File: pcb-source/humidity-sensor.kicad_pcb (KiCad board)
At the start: 2 copper layers, 34.3 x 22.6 mm, 78 parts, among them J1 Conn_ARM_JTAG_SWD_10, J2 Conn_02x03_Odd_Even, Q1 Q_NMOS_GSD, Q2 Q_NMOS_GSD, U1 STM32L051C8Tx, U2 SHTC3, U3 SYN115, Y1 13.56MHz, Y2 DNU

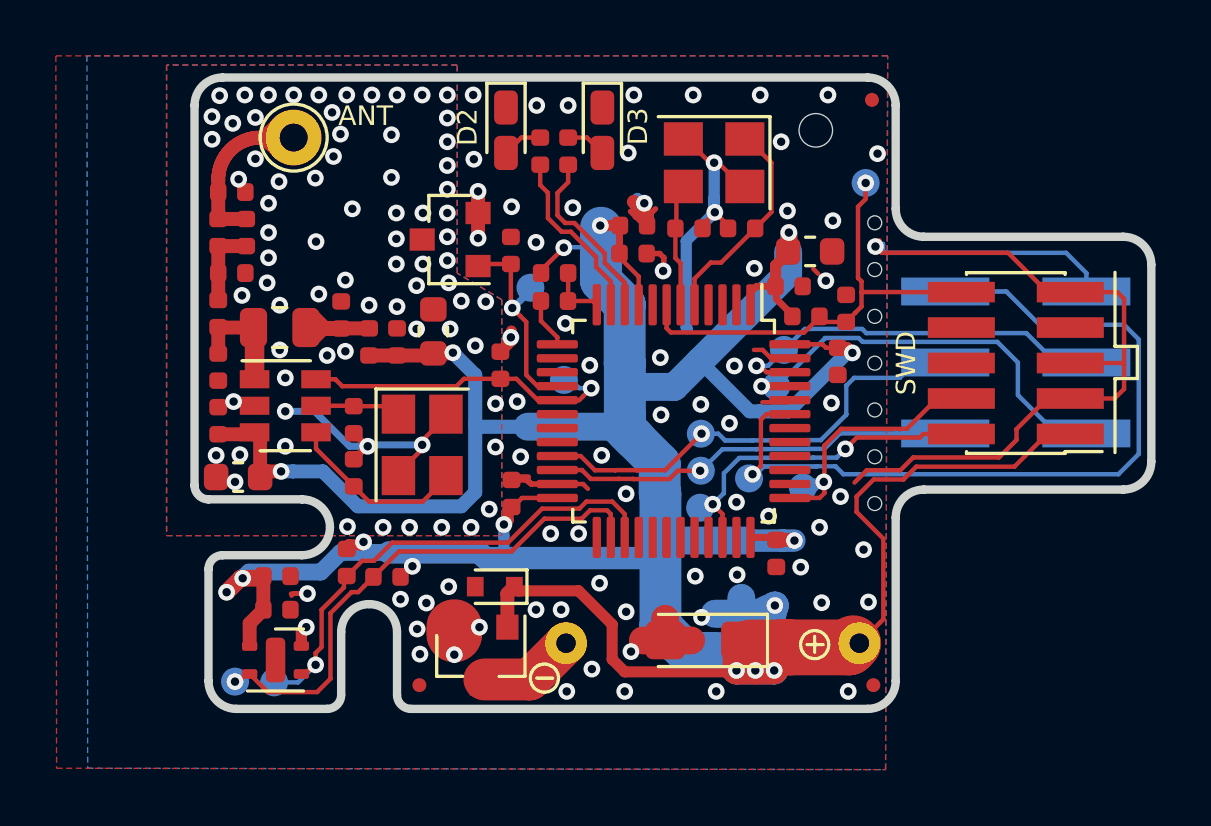
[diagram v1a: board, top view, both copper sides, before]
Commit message: Modify fiducials
Library footprint doesn't create copper pull-back from
soldermask opening.
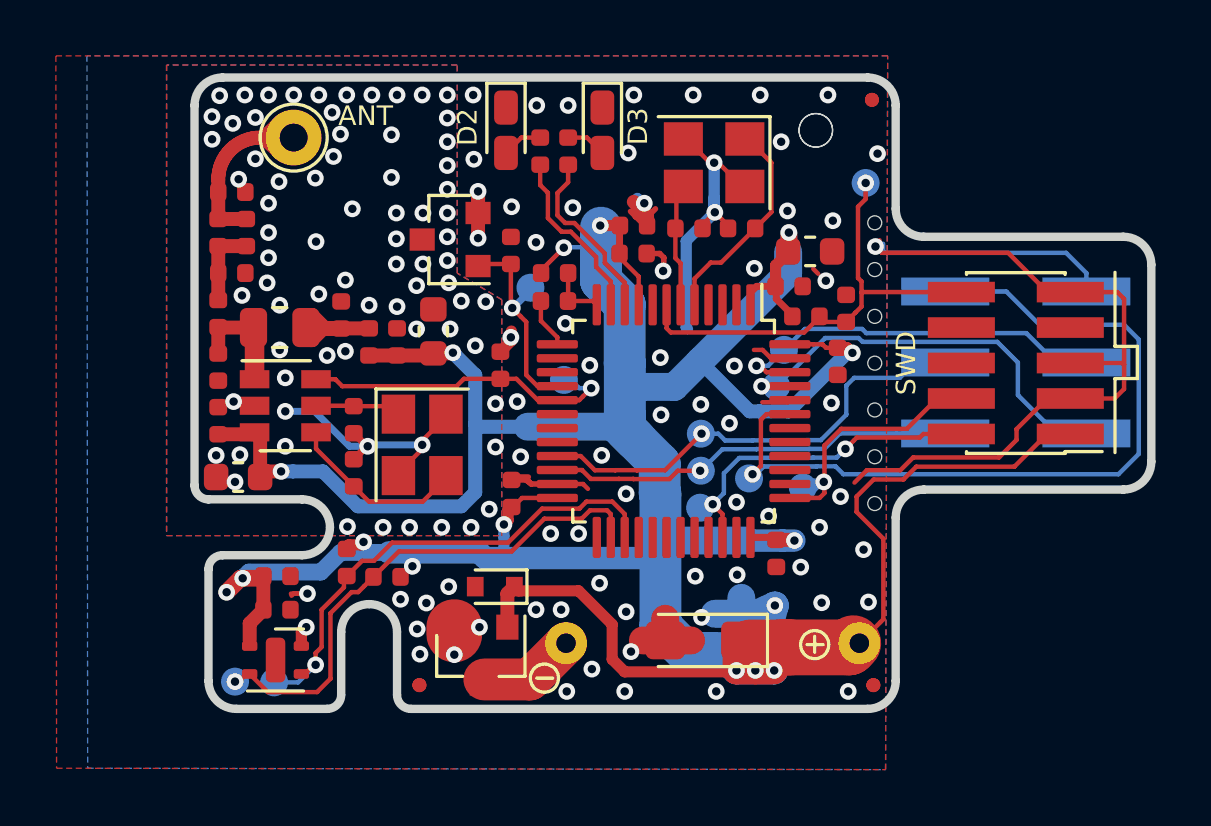
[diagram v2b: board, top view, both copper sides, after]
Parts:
- removed the FID1 at (62.7, 49.0)
- removed the FID2 at (79.0, 49.0)
- removed the FID3 at (78.9, 28.1)
- removed the REF** at (76.9, 29.2)
- added FID1 (x2): Fiducial, Fiducial:Fiducial_0.5mm_Mask1mm, F.Cu at (62.7, 49.0)
- added FID2 (x2): Fiducial, Fiducial:Fiducial_0.5mm_Mask1mm, F.Cu at (79.0, 49.0)
- added FID3 (x2): Fiducial, Fiducial:Fiducial_0.5mm_Mask1mm, F.Cu at (78.9, 28.1)
- added REF** (x2): NPTH-1.2mm, NPTH:NPTH-1.2mm, F.Cu at (76.9, 29.2)
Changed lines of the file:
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@@
       (drillshape 0)
       (scaleselection 1)
-      (outputdirectory "manual-gerbers2/"))
+      (outputdirectory "plot/"))
   )
   (net 0 "")
@@
     (add_net VCC)
   )
+  (module Fiducial:Fiducial_0.5mm_Mask1mm (layer F.Cu)
+    (at 78.9 28.1)
+    (descr "Circular Fiducial, 0.5mm bare copper, 1mm soldermask opening (Level C)")
+    (tags fiducial)
+    (attr smd)
+    (fp_text reference FID3 (at 0 -1.5) (layer F.SilkS) hide
+      (effects (font (size 1 1) (thickness 0.15)))
+    )
+    (fp_text value Fiducial (at 0 1.5) (layer F.Fab) hide
+      (effects (font (size 1 1) (thickness 0.15)))
+    )
+    (fp_circle (center 0 0) (end 0.75 0) (layer F.CrtYd) (width 0.05))
+    (fp_text user %R (at 0 0) (layer F.Fab)
+      (effects (font (size 0.2 0.2) (thickness 0.04)))
+    )
+    (fp_circle (center 0 0) (end 0.5 0) (layer F.Fab) (width 0.1))
+    (pad "" smd circle (at 0 0) (size 0.5 0.5) (layers F.Cu F.Mask)
+      (solder_mask_margin 0.25) (clearance 0.35))
+  )
+  (module Fiducial:Fiducial_0.5mm_Mask1mm (layer F.Cu)
+    (at 78.95 49.05)
+    (descr "Circular Fiducial, 0.5mm bare copper, 1mm soldermask opening (Level C)")
+    (tags fiducial)
+    (attr smd)
+    (fp_text reference FID2 (at 0 -1.5) (layer F.SilkS) hide
+      (effects (font (size 1 1) (thickness 0.15)))
+    )
+    (fp_text value Fiducial (at 0 1.5) (layer F.Fab) hide
+      (effects (font (size 1 1) (thickness 0.15)))
+    )
+    (fp_circle (center 0 0) (end 0.75 0) (layer F.CrtYd) (width 0.05))
+    (fp_text user %R (at 0 0) (layer F.Fab)
+      (effects (font (size 0.2 0.2) (thickness 0.04)))
+    )
+    (fp_circle (center 0 0) (end 0.5 0) (layer F.Fab) (width 0.1))
+    (pad "" smd circle (at 0 0) (size 0.5 0.5) (layers F.Cu F.Mask)
+      (solder_mask_margin 0.25) (clearance 0.35))
+  )
+  (module Fiducial:Fiducial_0.5mm_Mask1mm (layer F.Cu)
+    (at 62.7 49.05)
+    (descr "Circular Fiducial, 0.5mm bare copper, 1mm soldermask opening (Level C)")
+    (tags fiducial)
+    (attr smd)
+    (fp_text reference FID1 (at 0 -1.5) (layer F.SilkS) hide
+      (effects (font (size 1 1) (thickness 0.15)))
+    )
+    (fp_text value Fiducial (at 0 1.5) (layer F.Fab) hide
+      (effects (font (size 1 1) (thickness 0.15)))
+    )
+    (fp_circle (center 0 0) (end 0.75 0) (layer F.CrtYd) (width 0.05))
+    (fp_text user %R (at 0 0) (layer F.Fab)
+      (effects (font (size 0.2 0.2) (thickness 0.04)))
+    )
+    (fp_circle (center 0 0) (end 0.5 0) (layer F.Fab) (width 0.1))
+    (pad "" smd circle (at 0 0) (size 0.5 0.5) (layers F.Cu F.Mask)
+      (solder_mask_margin 0.25) (clearance 0.35))
+  )
+  (module NPTH:NPTH-1.2mm (layer F.Cu)
+    (at 76.89 29.19)
+    (fp_text reference REF** (at 0.3 1.85) (layer F.SilkS) hide
+      (effects (font (size 1 1) (thickness 0.15)))
+    )
+    (fp_text value NPTH-1.2mm (at 0.6 -1.5) (layer F.Fab) hide
+      (effects (font (size 1 1) (thickness 0.15)))
+    )
+    (fp_circle (center 0 0) (end 0.85 0) (layer F.CrtYd) (width 0.05))
+    (pad "" np_thru_hole circle (at 0 0) (size 1.2 1.2) (drill 1.2) (layers *.Cu *.Mask))
+  )
   (module Symbol:OSHW-Symbol_6.7x6mm_Copper (layer B.Cu)

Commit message: Repour GND
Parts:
- removed the FID1 at (62.7, 49.0) (x2)
- removed the FID2 at (79.0, 49.0) (x2)
- removed the FID3 at (78.9, 28.1) (x2)
- removed the REF** at (76.9, 29.2) (x2)
- added FID1 (x2): Fiducial, Fiducial:Fiducial_0.5mm_Mask1mm, F.Cu at (62.7, 49.0)
- added FID2 (x2): Fiducial, Fiducial:Fiducial_0.5mm_Mask1mm, F.Cu at (79.0, 49.0)
- added FID3 (x2): Fiducial, Fiducial:Fiducial_0.5mm_Mask1mm, F.Cu at (78.9, 28.1)
- added REF** (x2): NPTH-1.2mm, NPTH:NPTH-1.2mm, F.Cu at (76.9, 29.2)
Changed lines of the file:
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@@
     (tracks 783)
     (zones 0)
-    (modules 78)
+    (modules 82)
     (nets 55)
   )
@@
   )
   (layers
-    (0 F.Cu signal hide)
-    (31 B.Cu signal hide)
-    (32 B.Adhes user hide)
-    (33 F.Adhes user hide)
-    (34 B.Paste user hide)
-    (35 F.Paste user hide)
-    (36 B.SilkS user hide)
-    (37 F.SilkS user hide)
-    (38 B.Mask user hide)
-    (39 F.Mask user hide)
-    (40 Dwgs.User user hide)
-    (41 Cmts.User user hide)
-    (42 Eco1.User user hide)
-    (43 Eco2.User user hide)
-    (44 Edge.Cuts user hide)
-    (45 Margin user hide)
-    (46 B.CrtYd user hide)
-    (47 F.CrtYd user hide)
+    (0 F.Cu signal)
+    (31 B.Cu signal)
+    (32 B.Adhes user)
+    (33 F.Adhes user)
+    (34 B.Paste user)
+    (35 F.Paste user)
+    (36 B.SilkS user)
+    (37 F.SilkS user)
+    (38 B.Mask user)
+    (39 F.Mask user)
+    (40 Dwgs.User user)
+    (41 Cmts.User user)
+    (42 Eco1.User user)
+    (43 Eco2.User user)
+    (44 Edge.Cuts user)
+    (45 Margin user)
+    (46 B.CrtYd user)
+    (47 F.CrtYd user)
     (48 B.Fab user)
-    (49 F.Fab user hide)
+    (49 F.Fab user)
   )
   (setup
